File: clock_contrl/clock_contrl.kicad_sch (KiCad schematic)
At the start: 21 parts, among them J1 RJ45, J10 Screw_Terminal_01x03, J11 Conn_01x03_Pin, J2 USB_C_Receptacle_PowerOnly_6P, J3 Conn_01x04_Socket, J6 Conn_01x16_Socket, J7 Conn_01x08_Socket, J8 Conn_01x04_Pin, J9 Conn_01x08_Socket, SW1 RotaryEncoder_Switch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

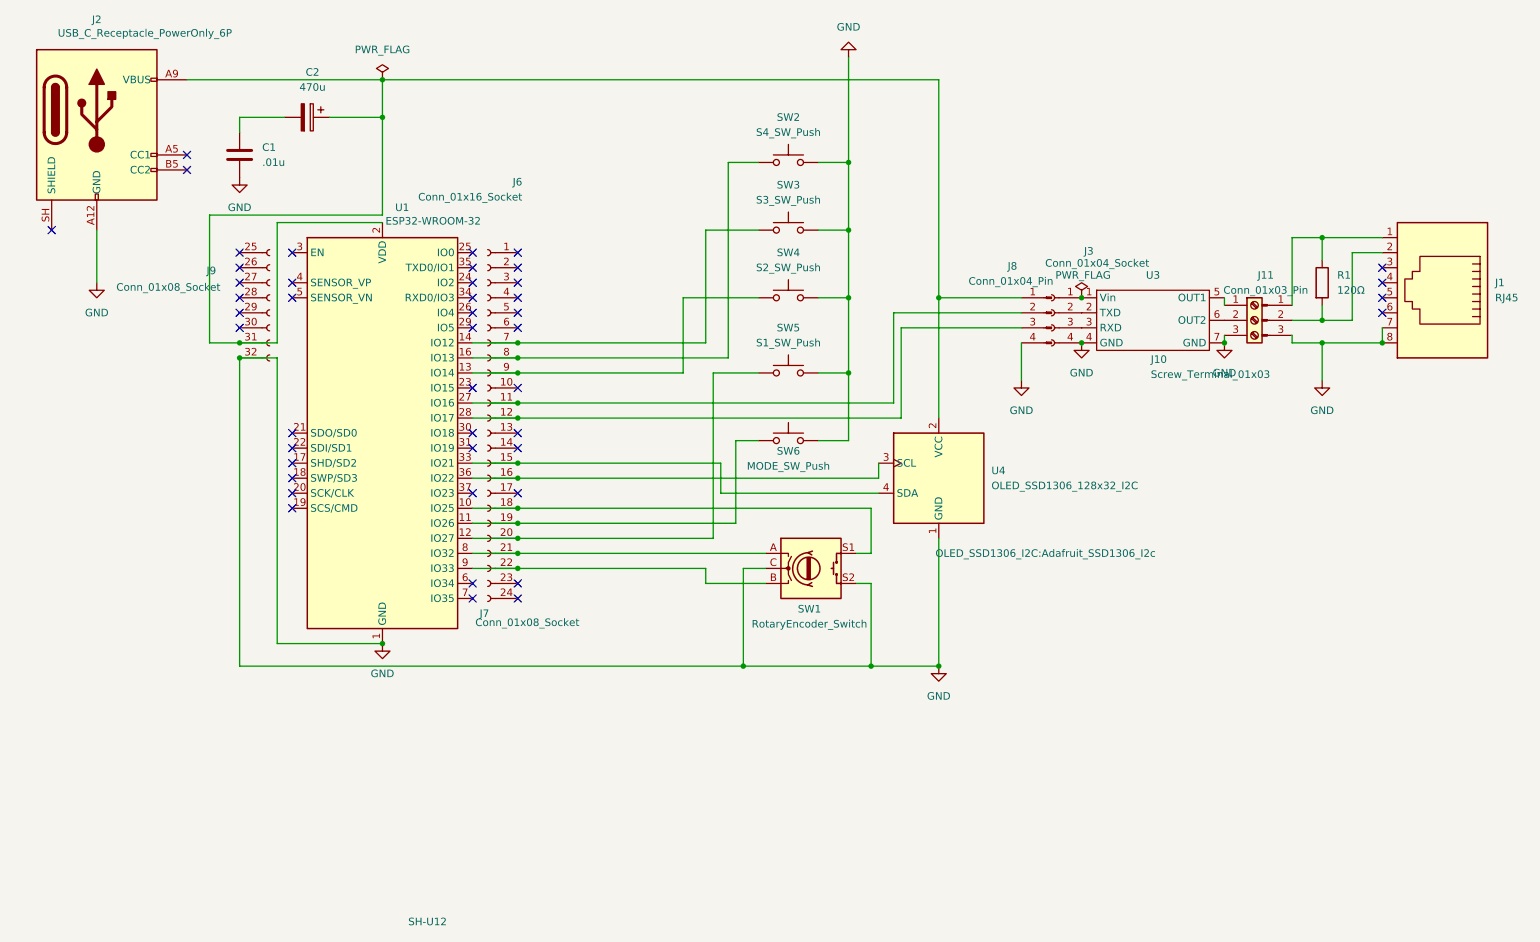
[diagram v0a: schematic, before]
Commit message: コントロールボックスの基盤を完成しました
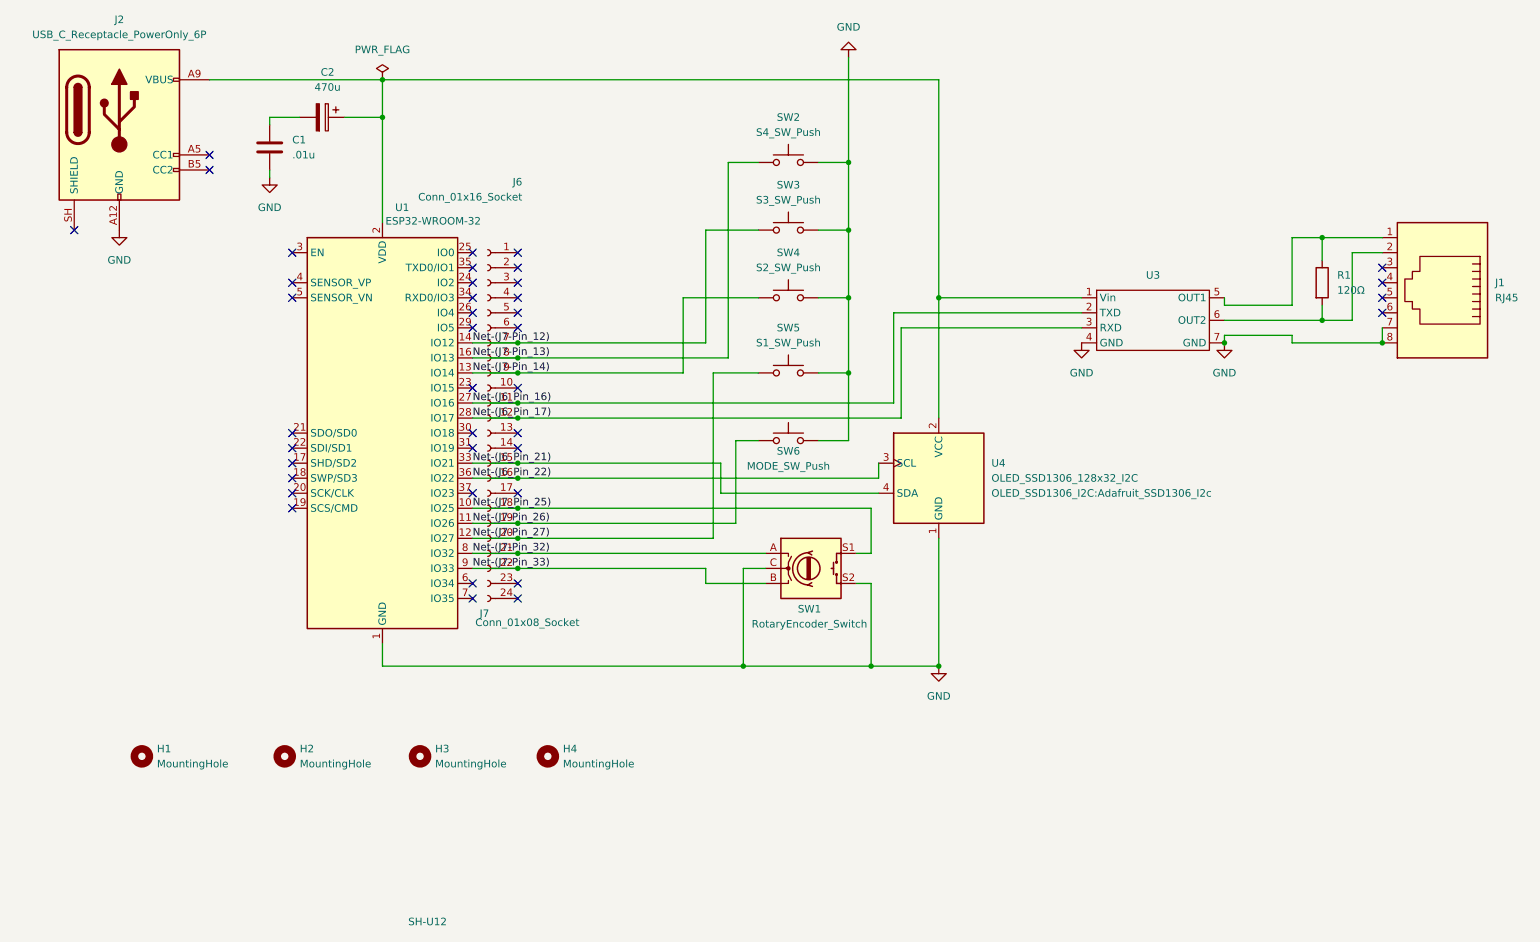
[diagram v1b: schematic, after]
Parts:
- removed J10: Screw_Terminal_01x03, symbol Connector:Screw_Terminal_01x03
- removed J11: Conn_01x03_Pin, symbol Connector:Conn_01x03_Pin
- removed J3: Conn_01x04_Socket, Connector_PinSocket_2.54mm:PinSocket_1x04_P2.54mm_Vertical, symbol Connector:Conn_01x04_Socket
- removed J8: Conn_01x04_Pin, symbol Connector:Conn_01x04_Pin
- removed J9: Conn_01x08_Socket, symbol Connector:Conn_01x08_Socket
- added H1, H2, H3, H4: MountingHole, MountingHole:MountingHole_3mm, symbol Mechanical:MountingHole
- C1, C2: KiLib_Generator (none) -> capacitor/THT/other
- J6, J7: KiLib_Generator (none) -> connector/pin_header_socket
- R1: KiLib_Generator (none) -> resistor/THT
- U1: footprint RF_Module:ESP32-WROOM-32 -> (none)
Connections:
- net at J1.1, R1.1: now also U3.5 (OUT1)
- net at J1.2, R1.2: now also U3.6 (OUT2)
- net Net-(J7-Pin_26): now reaches J7.19 (Pin_3), SW6.1, U1.11 (IO26)
- net Net-(J7-Pin_27): now reaches J7.20 (Pin_4), SW5.1, U1.12 (IO27)
- net Net-(J7-Pin_14): now reaches J6.9 (Pin_9), SW4.1, U1.13 (IO14)
- net at C2.1, J2.A9 (VBUS), J2.B9 (VBUS)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: now also U3.1 (Vin)
- net Net-(J6_Pin_16): now reaches J6.11 (Pin_11), U1.27 (IO16)
- net Net-(J6_Pin_16): now also U3.2 (TXD)
- net Net-(J6_Pin_17): now reaches J6.12 (Pin_12), U1.28 (IO17)
- net Net-(J6_Pin_17): now also U3.3 (RXD)
- net Net-(J7-Pin_12): now reaches J6.7 (Pin_7), SW3.1, U1.14 (IO12)
- net Net-(J6_Pin_21): now reaches J6.15 (Pin_15), U1.33 (IO21), U4.4 (SDA)
- net Net-(J6_Pin_22): now reaches J6.16 (Pin_16), U1.36 (IO22), U4.3 (SCL)
- net Net-(J7-Pin_13): now reaches J6.8 (Pin_8), SW2.1, U1.16 (IO13)
- net Net-(J7_Pin_25): now reaches J7.18 (Pin_2), SW1.S1, U1.10 (IO25)
- net Net-(J7-Pin_32): now reaches J7.21 (Pin_5), SW1.A, U1.8 (IO32)
- net Net-(J7-Pin_33): now reaches J7.22 (Pin_6), SW1.B, U1.9 (IO33)
- no-connect marks 46 -> 40
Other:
- moved on the sheet: C1, C2

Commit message: 基盤のUSB端子とRJ45端子を実際のフットプリントに変更しました。
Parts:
- J1: footprint Connector_RJ:RJ45_Abracon_ARJP11A-MA_Horizontal -> Connector_RJ:RJ45_Amphenol_54602-x08_Horizontal
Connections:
- net GND: now also J2.SH (SHIELD)
- net Net-(J11-Pin_1): now reaches J1.1, R1.1, U3.5 (OUT1)
- net Net-(J11-Pin_2): now reaches J1.2, R1.2, U3.6 (OUT2)
- net Net-(J6_Pin_22) renamed Net-(J6-Pin_16)
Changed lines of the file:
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@@
+		)
+	)
+	(label "Net-(J11-Pin_2)"
+		(at 245.11 72.39 180)
+		(effects
+			(font
+				(size 1.27 1.27)
+			)
+			(justify right bottom)
 		)
 	)
@@
 		)
 	)
+	(label "Net-(J11-Pin_1)"
+		(at 245.11 69.85 180)
+		(effects
+			(font
+				(size 1.27 1.27)
+			)
+			(justify right bottom)
+		)
+	)
+	(label "Net-(J11-Pin_1)"
+		(at 245.11 69.85 180)
+		(effects
+			(font
+				(size 1.27 1.27)
+			)
+			(justify right bottom)
+		)
+	)
 	(label "Net-(J7-Pin_26)"
 		(at 91.44 118.11 0)
@@
 		)
 	)
-	(label "Net-(J6_Pin_22)"
+	(label "Net-(J6-Pin_16)"
 		(at 91.44 110.49 0)
 		(effects
@@
 		)
 	)
+	(label "Net-(J11-Pin_2)"
+		(at 245.11 72.39 180)
+		(effects
+			(font
+				(size 1.27 1.27)
+			)
+			(justify right bottom)
+		)
+	)
 	(label "Net-(J6_Pin_21)"
 		(at 91.44 107.95 0)
@@
 		)
 	)
+	(label "GND"
+		(at 24.13 68.58 270)
+		(effects
+			(font
+				(size 1.27 1.27)
+			)
+			(justify right bottom)
+		)
+	)
 	(label "Net-(J7-Pin_14)"
 		(at 91.44 92.71 0)
@@
 			)
 		)
-		(property "Footprint" "Connector_RJ:RJ45_Abracon_ARJP11A-MA_Horizontal"
+		(property "Footprint" "Connector_RJ:RJ45_Amphenol_54602-x08_Horizontal"
 			(at 255.27 78.105 90)
 			(hide yes)
